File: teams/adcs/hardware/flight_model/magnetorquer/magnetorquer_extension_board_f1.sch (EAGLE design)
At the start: 6 parts

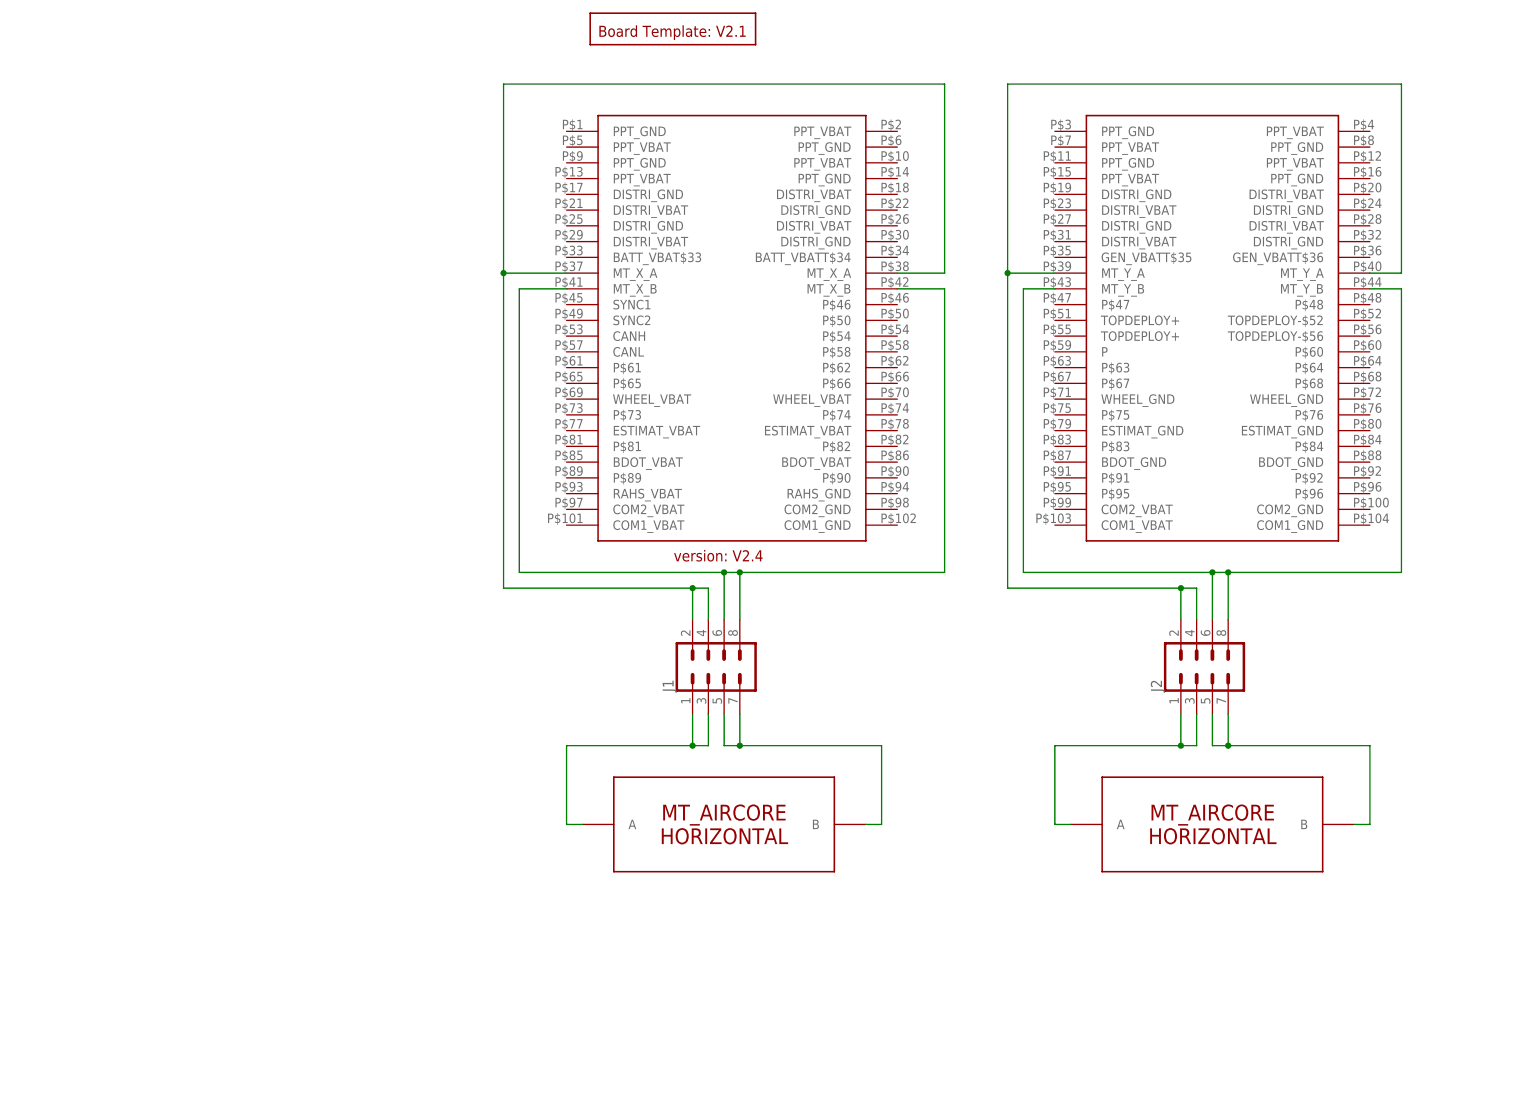
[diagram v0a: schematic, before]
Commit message: added umbilical and com2 connector
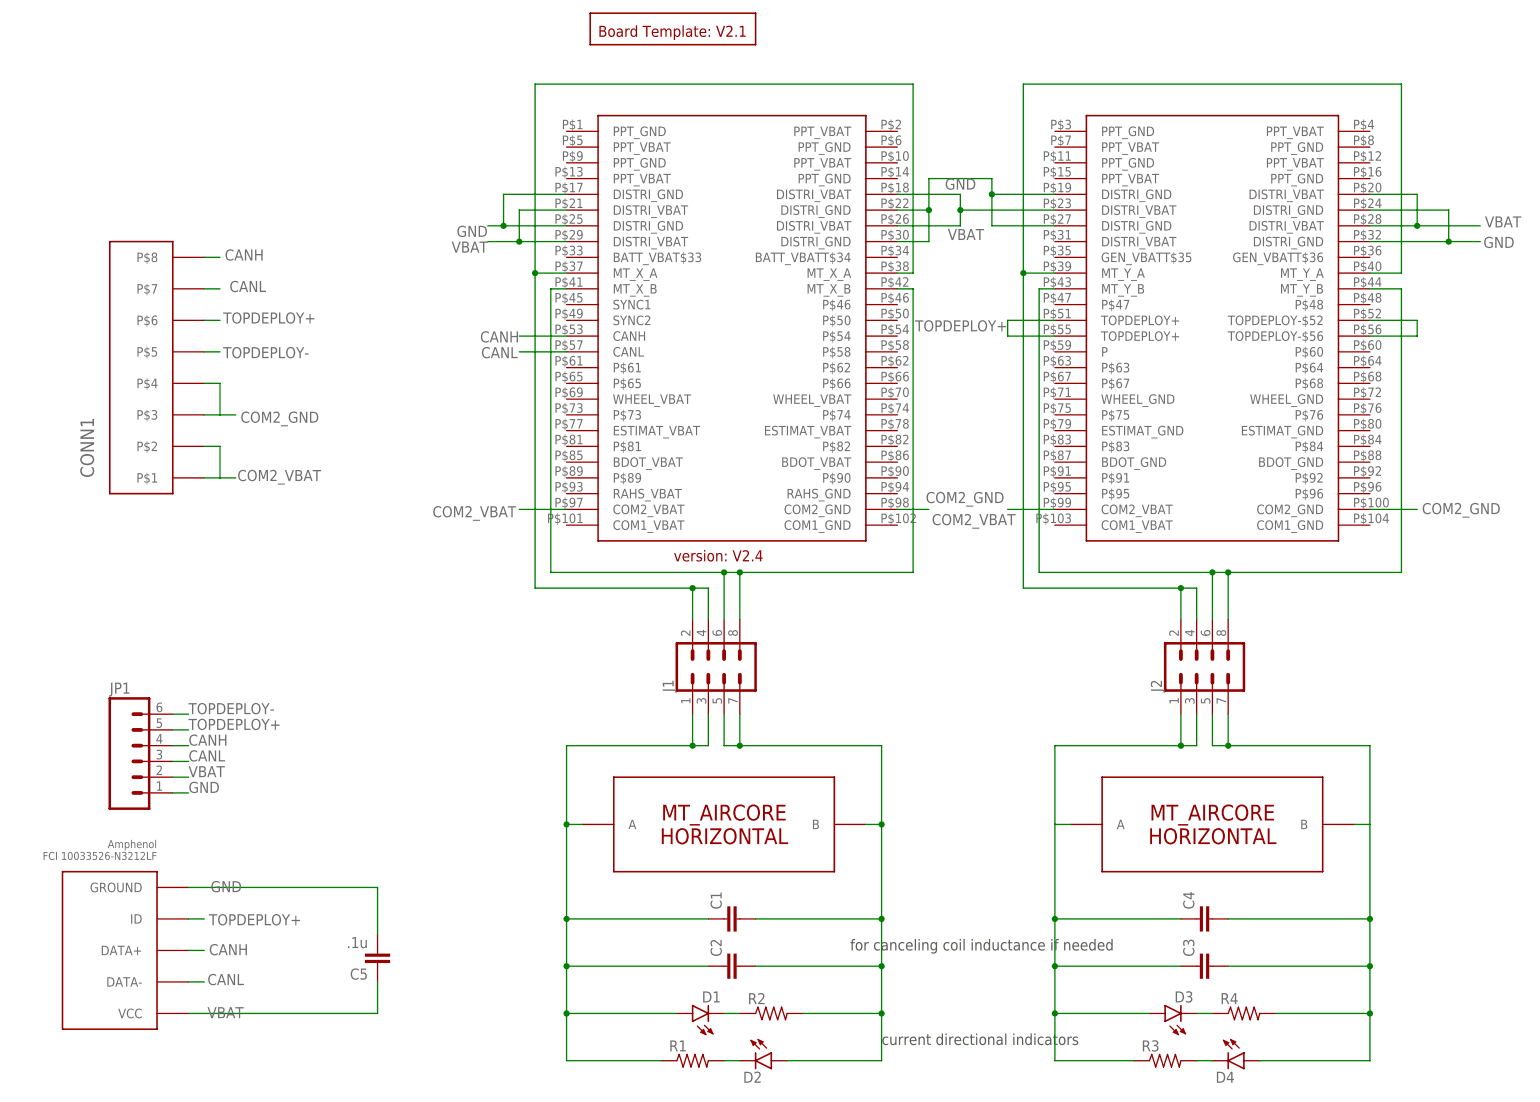
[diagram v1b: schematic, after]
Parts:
- added C1, C4: (no value), DubSat1 Components:CAPACITOR0805
- added C2, C3: (no value), DubSat1 Components:CAPACITOR1210
- added C5: .1u, DubSat1 Components:CAPACITOR0805
- added CONN1: PICOLOCK_8PICOLOCK_8, DubSat1 Components:PICOLOCK_8PICOLOCK_8
- added D1, D2, D3, D4: (no value), DubSat1 Components:LED
- added JP1: (no value), SparkFun-Connectors:M06LOCK
- added R1, R2, R3, R4: (no value), DubSat1 Components:RESISTOR0805
- added U$3: USB_MINI-B_AMPHENOL, I_O_connectors:USB_MINI-B_AMPHENOL
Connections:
- new net CANH: CONN1.P$8, JP1.4, U$1.CANH, U$3.DATA+
- new net CANL: CONN1.P$7, JP1.3, U$1.CANL, U$3.DATA-
- new net COM2_GND: CONN1.P$3, CONN1.P$4, U$1.COM2_GND@100, U$1.COM2_GND@98
- new net COM2_VBAT: CONN1.P$1, CONN1.P$2, U$1.COM2_VBAT@97, U$1.COM2_VBAT@99
- new net GND: C5.2, JP1.1, U$1.DISTRI_GND@17, U$1.DISTRI_GND@19, U$1.DISTRI_GND@22, U$1.DISTRI_GND@24, U$1.DISTRI_GND@25, U$1.DISTRI_GND@27, U$1.DISTRI_GND@30, U$1.DISTRI_GND@32, U$3.GROUND
- new net N$2: D1.C, R2.1
- new net N$3: D2.C, R1.2
- new net N$4: D3.C, R4.1
- new net N$5: D4.C, R3.2
- new net TOPDEPLOY+: CONN1.P$6, JP1.5, U$1.TOPDEPLOY+@51, U$1.TOPDEPLOY+@55, U$3.ID
- new net TOPDEPLOY-: CONN1.P$5, JP1.6, U$1.TOPDEPLOY-$52, U$1.TOPDEPLOY-$56
- new net VBAT: C5.1, JP1.2, U$1.DISTRI_VBAT@18, U$1.DISTRI_VBAT@20, U$1.DISTRI_VBAT@21, U$1.DISTRI_VBAT@23, U$1.DISTRI_VBAT@26, U$1.DISTRI_VBAT@28, U$1.DISTRI_VBAT@29, U$3.VCC
- net MT_X_A: now also C3.1, C4.1, D3.A, J2.1, J2.3, MT_Y.A, R3.1; no longer J1.1, J1.3, MT_X.A
- net MT_X_A_STACK: now also J2.2, J2.4, U$1.MT_Y_A@1, U$1.MT_Y_A@2; no longer J1.2, J1.4, U$1.MT_X_A@1, U$1.MT_X_A@2
- net MT_X_B: now also C3.2, C4.2, D4.A, J2.5, J2.7, MT_Y.B, R4.2; no longer J1.5, J1.7, MT_X.B
- net MT_X_B_STACK: now also J2.6, J2.8, U$1.MT_Y_B@1, U$1.MT_Y_B@2; no longer J1.6, J1.8, U$1.MT_X_B@1, U$1.MT_X_B@2
- net MT_Y_A: now also C1.1, C2.1, D1.A, J1.1, J1.3, MT_X.A, R1.1; no longer J2.1, J2.3, MT_Y.A
- net MT_Y_A_STACK: now also J1.2, J1.4, U$1.MT_X_A@1, U$1.MT_X_A@2; no longer J2.2, J2.4, U$1.MT_Y_A@1, U$1.MT_Y_A@2
- net MT_Y_B: now also C1.2, C2.2, D2.A, J1.5, J1.7, MT_X.B, R2.2; no longer J2.5, J2.7, MT_Y.B
- net MT_Y_B_STACK: now also J1.6, J1.8, U$1.MT_X_B@1, U$1.MT_X_B@2; no longer J2.6, J2.8, U$1.MT_Y_B@1, U$1.MT_Y_B@2
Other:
- note added: "current directional indicators"
- note added: "for canceling coil inductance if needed"

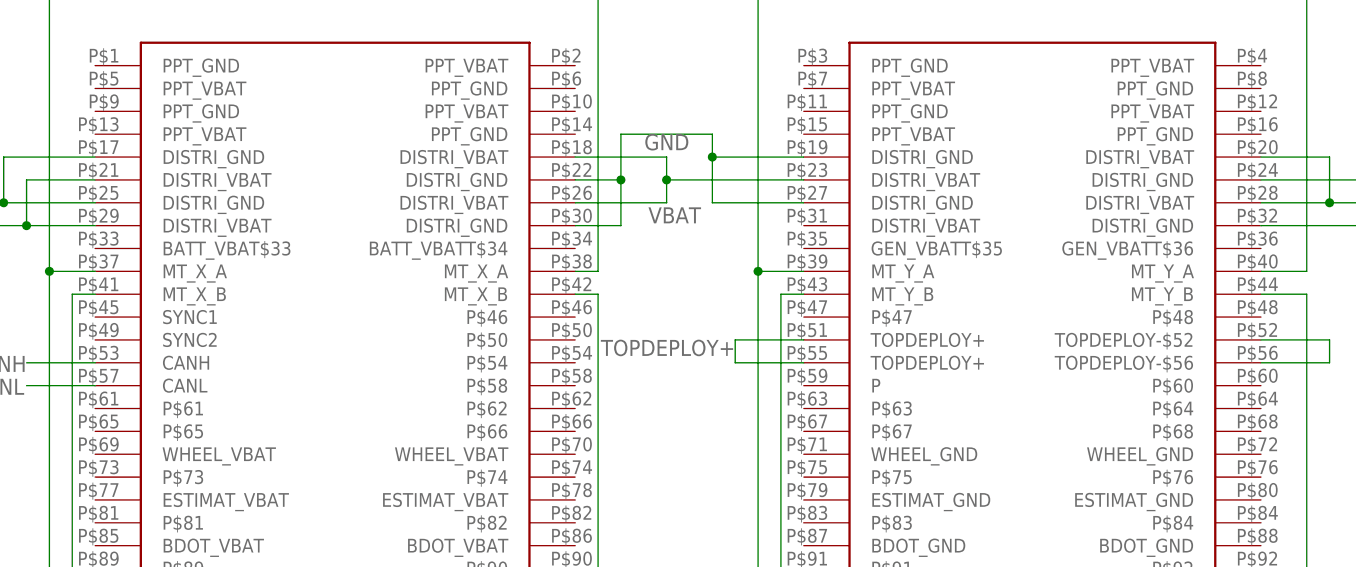
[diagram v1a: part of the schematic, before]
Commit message: PC104 connector change: switched X and Y pin assignments, MQT board: converted to 4 layer board, layer 4 GND, previous layer 2 traces moved to new layer 2; added X and Y MQT outputs; added 3x LDOs
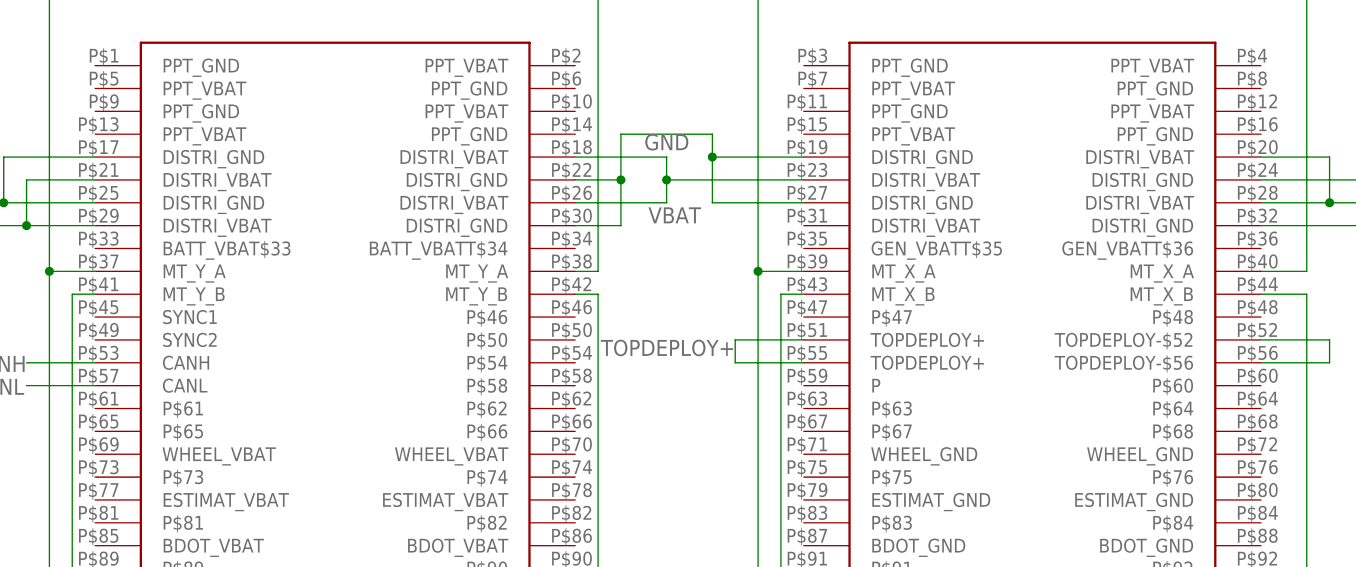
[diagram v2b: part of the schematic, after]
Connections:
- net MT_X_A_STACK: now also U$1.MT_X_A@39, U$1.MT_X_A@40; no longer U$1.MT_Y_A@1, U$1.MT_Y_A@2
- net MT_X_B_STACK: now also U$1.MT_X_B@43, U$1.MT_X_B@44; no longer U$1.MT_Y_B@1, U$1.MT_Y_B@2
- net MT_Y_A_STACK: now also U$1.MT_Y_A@37, U$1.MT_Y_A@38; no longer U$1.MT_X_A@1, U$1.MT_X_A@2
- net MT_Y_B_STACK: now also U$1.MT_Y_B@41, U$1.MT_Y_B@42; no longer U$1.MT_X_B@1, U$1.MT_X_B@2
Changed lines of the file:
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@@
 <wire x1="68.58" y1="-5.08" x2="68.58" y2="45.72" width="0.1524" layer="91"/>
 <junction x="93.98" y="-5.08"/>
-<pinref part="U$1" gate="G$1" pin="MT_Y_A@1"/>
+<pinref part="U$1" gate="G$1" pin="MT_X_A@39"/>
 <wire x1="68.58" y1="45.72" x2="73.66" y2="45.72" width="0.1524" layer="91"/>
 <wire x1="68.58" y1="45.72" x2="68.58" y2="76.2" width="0.1524" layer="91"/>
@@
 <wire x1="68.58" y1="76.2" x2="129.54" y2="76.2" width="0.1524" layer="91"/>
 <wire x1="129.54" y1="76.2" x2="129.54" y2="45.72" width="0.1524" layer="91"/>
-<pinref part="U$1" gate="G$1" pin="MT_Y_A@2"/>
+<pinref part="U$1" gate="G$1" pin="MT_X_A@40"/>
 <wire x1="129.54" y1="45.72" x2="124.46" y2="45.72" width="0.1524" layer="91"/>
 </segment>
@@
 <wire x1="129.54" y1="-2.54" x2="129.54" y2="43.18" width="0.1524" layer="91"/>
 <junction x="101.6" y="-2.54"/>
-<pinref part="U$1" gate="G$1" pin="MT_Y_B@2"/>
+<pinref part="U$1" gate="G$1" pin="MT_X_B@44"/>
 <wire x1="129.54" y1="43.18" x2="124.46" y2="43.18" width="0.1524" layer="91"/>
 <junction x="99.06" y="-2.54"/>
 <wire x1="99.06" y1="-2.54" x2="71.12" y2="-2.54" width="0.1524" layer="91"/>
 <wire x1="71.12" y1="-2.54" x2="71.12" y2="43.18" width="0.1524" layer="91"/>
-<pinref part="U$1" gate="G$1" pin="MT_Y_B@1"/>
+<pinref part="U$1" gate="G$1" pin="MT_X_B@43"/>
 <wire x1="71.12" y1="43.18" x2="73.66" y2="43.18" width="0.1524" layer="91"/>
 </segment>
@@
 <wire x1="50.8" y1="-2.54" x2="50.8" y2="43.18" width="0.1524" layer="91"/>
 <junction x="22.86" y="-2.54"/>
-<pinref part="U$1" gate="G$1" pin="MT_X_B@2"/>
+<pinref part="U$1" gate="G$1" pin="MT_Y_B@42"/>
 <wire x1="50.8" y1="43.18" x2="48.26" y2="43.18" width="0.1524" layer="91"/>
 <junction x="20.32" y="-2.54"/>
 <wire x1="20.32" y1="-2.54" x2="-7.62" y2="-2.54" width="0.1524" layer="91"/>
-<pinref part="U$1" gate="G$1" pin="MT_X_B@1"/>
+<pinref part="U$1" gate="G$1" pin="MT_Y_B@41"/>
 <wire x1="-7.62" y1="-2.54" x2="-7.62" y2="43.18" width="0.1524" layer="91"/>
 <wire x1="-7.62" y1="43.18" x2="-5.08" y2="43.18" width="0.1524" layer="91"/>
@@
 <junction x="15.24" y="-5.08"/>
 <wire x1="-10.16" y1="-5.08" x2="-10.16" y2="45.72" width="0.1524" layer="91"/>
-<pinref part="U$1" gate="G$1" pin="MT_X_A@1"/>
+<pinref part="U$1" gate="G$1" pin="MT_Y_A@37"/>
 <wire x1="-10.16" y1="45.72" x2="-5.08" y2="45.72" width="0.1524" layer="91"/>
 <wire x1="-10.16" y1="45.72" x2="-10.16" y2="76.2" width="0.1524" layer="91"/>
@@
 <junction x="-10.16" y="45.72"/>
 <wire x1="50.8" y1="76.2" x2="50.8" y2="45.72" width="0.1524" layer="91"/>
-<pinref part="U$1" gate="G$1" pin="MT_X_A@2"/>
+<pinref part="U$1" gate="G$1" pin="MT_Y_A@38"/>
 <wire x1="50.8" y1="45.72" x2="48.26" y2="45.72" width="0.1524" layer="91"/>
 </segment>
